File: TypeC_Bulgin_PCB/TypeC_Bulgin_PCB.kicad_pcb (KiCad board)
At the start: 2 copper layers, 16.3 x 17.3 mm, 4 parts, among them J1 Conn_01x01_Female, J3 Conn_01x13, J4 Conn_01x13, J6 USB_C_Receptacle

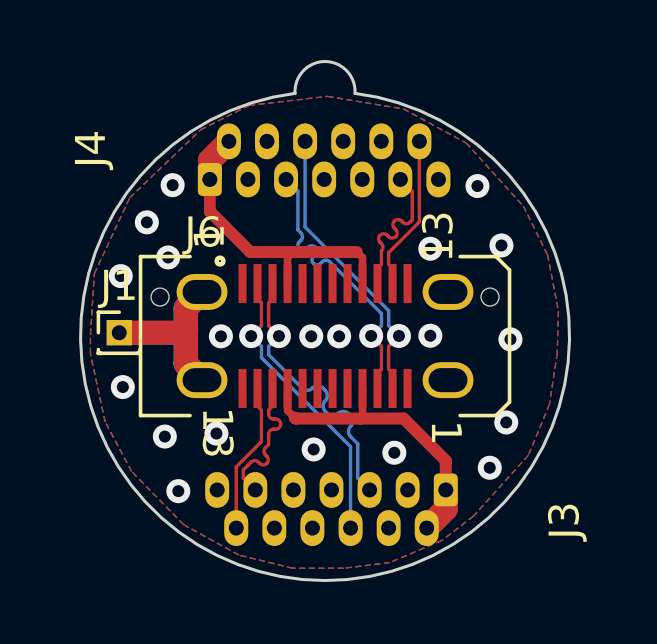
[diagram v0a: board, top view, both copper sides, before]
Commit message: v0.62 DRC errors were corrected, Gerbers, drl were updated
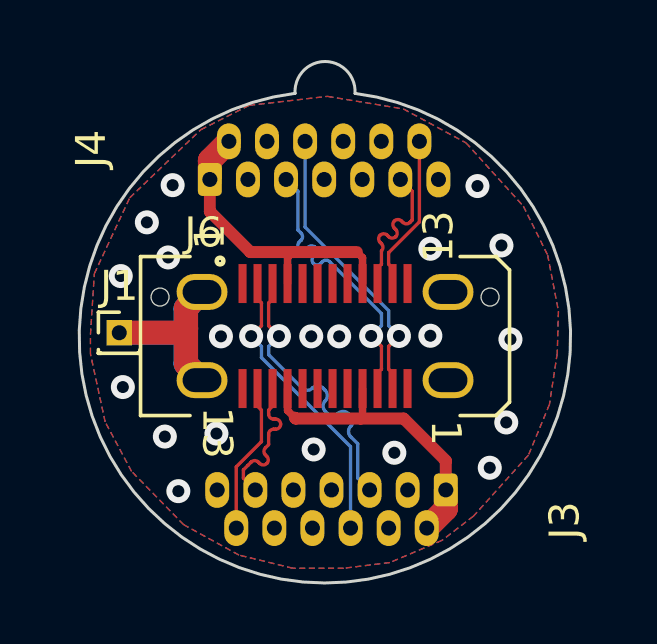
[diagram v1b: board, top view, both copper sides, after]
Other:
- board size 16.3 x 17.3 mm -> 16.4 x 17.4 mm
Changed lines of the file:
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@@
   )
   (gr_arc locked (start 99 91.91) (mid 100.000611 90.848202) (end 100.999926 91.91122) (layer "Edge.Cuts") (width 0.1))
-  (gr_arc (start 100.999926 91.911221) (mid 99.999345 108.15035) (end 99.001366 91.911061) (layer "Edge.Cuts") (width 0.1))
+  (gr_arc (start 100.999926 91.911221) (mid 99.989998 108.231514) (end 99 91.91) (layer "Edge.Cuts") (width 0.1))
   (via (at 105.08 95) (size 0.8) (drill 0.4) (layers "F.Cu" "B.Cu") (free) (net 1))
   (via (at 106.04 102.88) (size 0.8) (drill 0.4) (layers "F.Cu" "B.Cu") (free) (net 1))

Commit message: v0.63 geometry was corrected, gerbers, DRC, drl
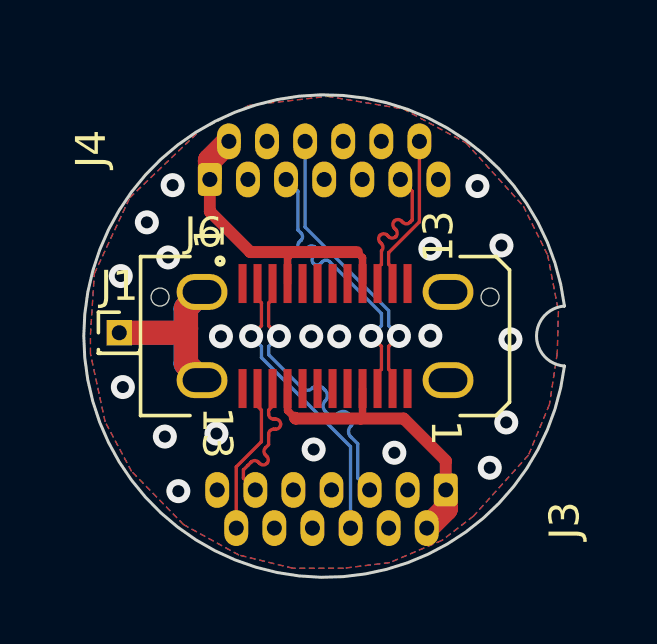
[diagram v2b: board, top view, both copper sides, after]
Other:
- board size 16.4 x 17.4 mm -> 16 x 16.1 mm
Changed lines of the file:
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@@
     )
   )
-  (gr_arc locked (start 99 91.91) (mid 100.000611 90.848202) (end 100.999926 91.91122) (layer "Edge.Cuts") (width 0.1))
-  (gr_arc (start 100.999926 91.911221) (mid 99.989998 108.231514) (end 99 91.91) (layer "Edge.Cuts") (width 0.1))
+  (gr_arc (start 107.979999 101) (mid 91.957588 100.000038) (end 107.97999 98.999924) (layer "Edge.Cuts") (width 0.1))
+  (gr_arc (start 107.979999 101) (mid 107.048829 99.999966) (end 107.97999 98.999924) (layer "Edge.Cuts") (width 0.1))
+  (dimension (type aligned) (layer "Dwgs.User")
+    (pts (xy 100 91.96) (xy 100 107.99))
+    (height 11.23)
+    (gr_text "16,0300 мм" (at 87.62 99.975 90) (layer "Dwgs.User")
+      (effects (font (size 1 1) (thickness 0.15)))
+    )
+    (format (units 3) (units_format 1) (precision 4))
+    (style (thickness 0.15) (arrow_length 1.27) (text_position_mode 0) (extension_height 0.58642) (extension_offset 0.5) keep_text_aligned)
+  )
+  (dimension (type center) (layer "Dwgs.User")
+    (pts (xy 100 100) (xy 100 90.58))
+    (style (thickness 0.15) (arrow_length 1.27) (text_position_mode 0) (extension_offset 0.5) keep_text_aligned)
+  )
   (via (at 105.08 95) (size 0.8) (drill 0.4) (layers "F.Cu" "B.Cu") (free) (net 1))
   (via (at 106.04 102.88) (size 0.8) (drill 0.4) (layers "F.Cu" "B.Cu") (free) (net 1))
